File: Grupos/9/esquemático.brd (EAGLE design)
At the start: 70.1 x 59.1 mm, 28 parts, among them Q1 MMBT4403LT1SMD, Q3 MMBT4403LT1SMD, U3 AP2210N-4.0TRG1, X1 MKDSN1,5/2-5,08, X2 MKDSN1,5/2-5,08, X3 MKDSN1,5/2-5,08, X4 MKDSN1,5/2-5,08

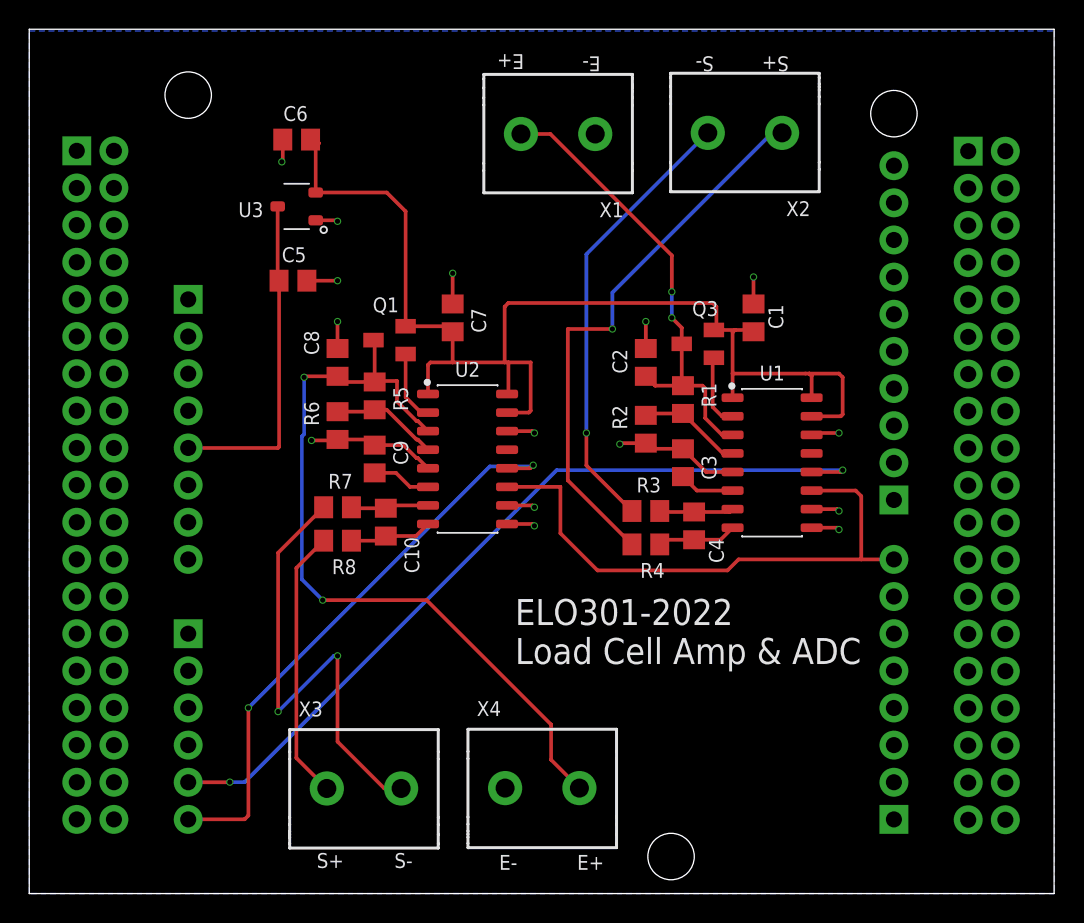
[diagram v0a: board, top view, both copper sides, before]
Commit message: Se cablean los ADC a SPI1 y SPI2
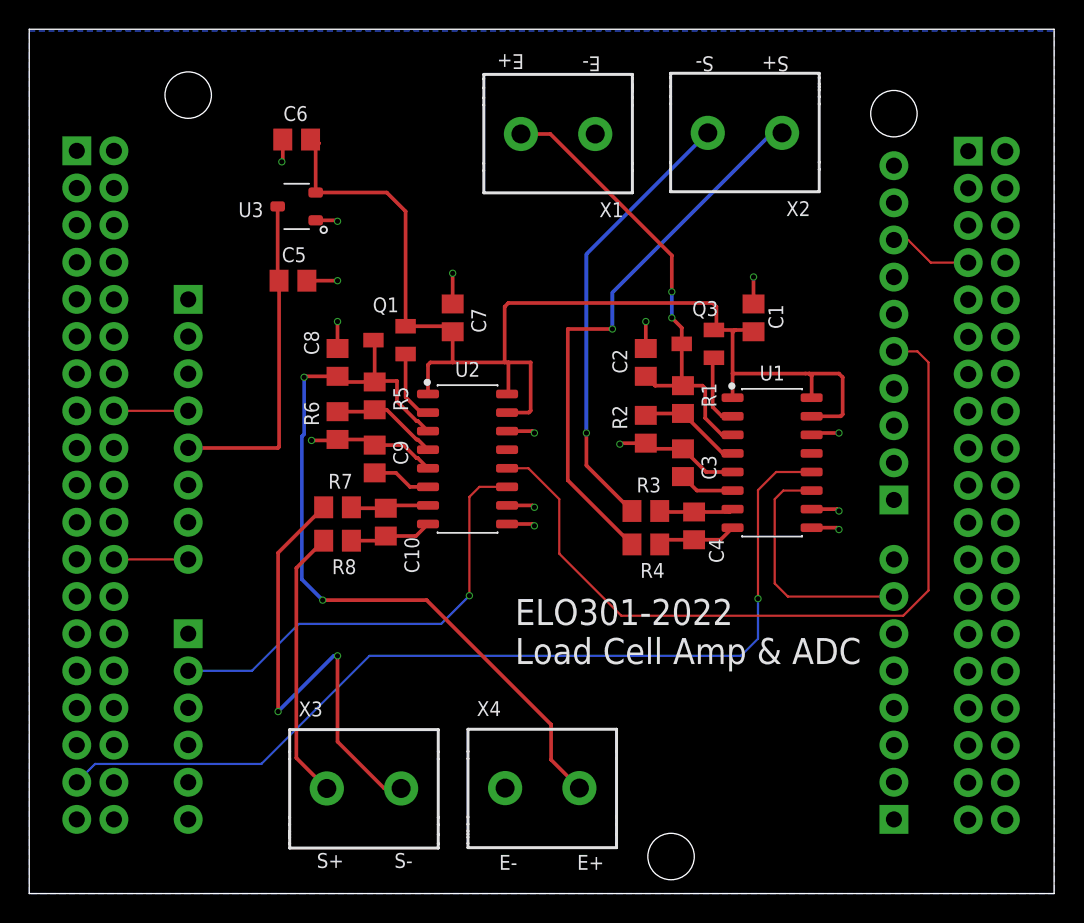
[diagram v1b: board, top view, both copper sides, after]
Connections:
- removed net N$20: M1.CN8-6, U2.12
- new net N$17: M1.CN5-5, U2.12
- new net N$21: M1.CN8-2, U2.11
- net N$19: now also M1.CN7-35; no longer M1.CN8-5
- net N$3: now also M1.CN9-7; no longer M1.CN9-8, U2.11
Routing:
- net N$17: track 0.00 -> 54.2 mm
- net N$20: track 40.0 -> 0.00 mm, vias 2 -> 0
- net N$21: track 0.00 -> 31.0 mm, vias 0 -> 1
- net N$3: track 38.9 -> 17.1 mm
- net N$19: track 55.8 -> 65.0 mm, vias 2 -> 1
- net AVDD: track 0.00 -> 5.72 mm
- net VIN: track 0.00 -> 5.08 mm
- net +3V3: track 0.00 -> 5.08 mm
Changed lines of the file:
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@@
 <contactref element="M1" pad="CN7-16"/>
 <contactref element="M1" pad="CN6-4"/>
-<wire x1="5.79" y1="33.012" x2="10.87" y2="33.012" width="0" layer="19" extent="1-1"/>
+<wire x1="5.79" y1="33.012" x2="10.87" y2="33.012" width="0.1524" layer="1"/>
 </signal>
 <signal name="+5V">
@@
 <contactref element="M1" pad="CN7-24"/>
 <contactref element="M1" pad="CN6-8"/>
-<wire x1="5.79" y1="22.852" x2="10.87" y2="22.852" width="0" layer="19" extent="1-1"/>
+<wire x1="5.79" y1="22.852" x2="10.87" y2="22.852" width="0.1524" layer="1"/>
 </signal>
 <signal name="VBAT">
@@
 <contactref element="M1" pad="CN5-8"/>
 <contactref element="M1" pad="CN10-7"/>
-<wire x1="59.13" y1="44.696" x2="64.21" y2="43.14700625" width="0" layer="19" extent="1-1"/>
+<wire x1="59.13" y1="44.696" x2="60.1044" y2="44.696" width="0.1524" layer="1"/>
+<wire x1="61.65339375" y1="43.14700625" x2="64.21" y2="43.14700625" width="0.1524" layer="1"/>
+<wire x1="60.1044" y1="44.696" x2="61.65339375" y2="43.14700625" width="0.1524" layer="1"/>
 </signal>
 <signal name="U5V">
@@
 <wire x1="25.738" y1="33.952" x2="25.738" y2="36.896" width="0.254" layer="1"/>
 <wire x1="26.67" y1="33.02" x2="25.738" y2="33.952" width="0.254" layer="1"/>
-</signal>
-<signal name="N$3">
-<contactref element="M1" pad="CN9-8"/>
-<contactref element="U1" pad="11"/>
-<contactref element="U2" pad="11"/>
-<wire x1="59.13" y1="22.852" x2="56.896" y2="22.852" width="0.254" layer="1"/>
-<wire x1="56.896" y1="22.852" x2="48.506" y2="22.852" width="0.254" layer="1"/>
-<wire x1="47.752" y1="22.098" x2="38.862" y2="22.098" width="0.254" layer="1"/>
-<wire x1="38.862" y1="22.098" x2="36.322" y2="24.638" width="0.254" layer="1"/>
-<wire x1="36.322" y1="24.638" x2="36.322" y2="27.813" width="0.254" layer="1"/>
-<wire x1="36.322" y1="27.813" x2="32.6753" y2="27.813" width="0.254" layer="1"/>
-<wire x1="48.506" y1="22.852" x2="47.752" y2="22.098" width="0.254" layer="1"/>
-<wire x1="53.5033" y1="27.559" x2="56.515" y2="27.559" width="0.254" layer="1"/>
-<wire x1="56.896" y1="27.178" x2="56.896" y2="22.852" width="0.254" layer="1"/>
-<wire x1="56.515" y1="27.559" x2="56.896" y2="27.178" width="0.254" layer="1"/>
-</signal>
-<signal name="N$19">
-<contactref element="U1" pad="12"/>
-<contactref element="M1" pad="CN8-5"/>
-<wire x1="10.87" y1="7.612" x2="13.708" y2="7.612" width="0.254" layer="1"/>
-<wire x1="13.708" y1="7.612" x2="13.716" y2="7.62" width="0.254" layer="1"/>
-<via x="13.716" y="7.62" extent="1-16" drill="0.35"/>
-<wire x1="13.716" y1="7.62" x2="14.732" y2="7.62" width="0.254" layer="16"/>
-<wire x1="36.068" y1="28.956" x2="14.732" y2="7.62" width="0.254" layer="16"/>
-<wire x1="36.068" y1="28.956" x2="55.626" y2="28.956" width="0.254" layer="16"/>
-<via x="55.626" y="28.956" extent="1-16" drill="0.35"/>
-<wire x1="55.626" y1="28.956" x2="55.499" y2="28.829" width="0.254" layer="1"/>
-<wire x1="55.499" y1="28.829" x2="53.5033" y2="28.829" width="0.254" layer="1"/>
-</signal>
-<signal name="N$20">
-<contactref element="M1" pad="CN8-6"/>
-<contactref element="U2" pad="12"/>
-<wire x1="10.87" y1="5.072" x2="10.878" y2="5.08" width="0.254" layer="1"/>
-<wire x1="10.878" y1="5.08" x2="14.732" y2="5.08" width="0.254" layer="1"/>
-<wire x1="14.732" y1="5.08" x2="14.986" y2="5.334" width="0.254" layer="1"/>
-<wire x1="14.986" y1="5.334" x2="14.986" y2="12.7" width="0.254" layer="1"/>
-<via x="14.986" y="12.7" extent="1-16" drill="0.35"/>
-<wire x1="31.496" y1="29.21" x2="32.512" y2="29.21" width="0.254" layer="16"/>
-<wire x1="14.986" y1="12.7" x2="31.496" y2="29.21" width="0.254" layer="16"/>
-<wire x1="32.512" y1="29.21" x2="34.544" y2="29.21" width="0.254" layer="16"/>
-<wire x1="34.544" y1="29.21" x2="34.46000625" y2="29.29399375" width="0.254" layer="16"/>
-<via x="34.46000625" y="29.29399375" extent="1-16" drill="0.35"/>
-<wire x1="34.46000625" y1="29.29399375" x2="34.2490125" y2="29.083" width="0.254" layer="1"/>
-<wire x1="34.2490125" y1="29.083" x2="32.6753" y2="29.083" width="0.254" layer="1"/>
 </signal>
 <signal name="N$22">
@@
 <wire x1="55.372" y1="35.56" x2="53.34" y2="35.56" width="0.254" layer="1"/>
 </signal>
+<signal name="N$17">
+<contactref element="U2" pad="12"/>
+<contactref element="M1" pad="CN5-5"/>
+<wire x1="59.13" y1="37.076" x2="60.7394" y2="37.076" width="0.1524" layer="1"/>
+<wire x1="60.7394" y1="37.076" x2="61.4934" y2="36.322" width="0.1524" layer="1"/>
+<wire x1="61.4934" y1="36.322" x2="61.4934" y2="20.7264" width="0.1524" layer="1"/>
+<wire x1="61.4934" y1="20.7264" x2="59.7662" y2="18.9992" width="0.1524" layer="1"/>
+<wire x1="34.1376" y1="29.083" x2="32.6753" y2="29.083" width="0.1524" layer="1"/>
+<wire x1="59.7662" y1="18.9992" x2="40.4876" y2="18.9992" width="0.1524" layer="1"/>
+<wire x1="40.4876" y1="18.9992" x2="36.2458" y2="23.241" width="0.1524" layer="1"/>
+<wire x1="36.2458" y1="23.241" x2="36.2458" y2="26.9748" width="0.1524" layer="1"/>
+<wire x1="36.2458" y1="26.9748" x2="34.1376" y2="29.083" width="0.1524" layer="1"/>
+</signal>
+<signal name="N$21">
+<contactref element="U2" pad="11"/>
+<contactref element="M1" pad="CN8-2"/>
+<wire x1="10.87" y1="15.232" x2="15.232" y2="15.232" width="0.1524" layer="16"/>
+<wire x1="28.1686" y1="18.4404" x2="30.099" y2="20.3708" width="0.1524" layer="16"/>
+<via x="30.099" y="20.3708" extent="1-16" drill="0.35"/>
+<wire x1="30.099" y1="20.3708" x2="30.099" y2="27.1272" width="0.1524" layer="1"/>
+<wire x1="30.7848" y1="27.813" x2="32.6753" y2="27.813" width="0.1524" layer="1"/>
+<wire x1="15.232" y1="15.232" x2="18.4404" y2="18.4404" width="0.1524" layer="16"/>
+<wire x1="18.4404" y1="18.4404" x2="28.1686" y2="18.4404" width="0.1524" layer="16"/>
+<wire x1="30.099" y1="27.1272" x2="30.7848" y2="27.813" width="0.1524" layer="1"/>
+</signal>
+<signal name="N$3">
+<contactref element="U1" pad="11"/>
+<contactref element="M1" pad="CN9-7"/>
+<wire x1="59.13" y1="20.312" x2="51.8748" y2="20.312" width="0.1524" layer="1"/>
+<wire x1="51.8748" y1="20.312" x2="50.9778" y2="21.209" width="0.1524" layer="1"/>
+<wire x1="50.9778" y1="21.209" x2="50.9778" y2="26.9748" width="0.1524" layer="1"/>
+<wire x1="51.562" y1="27.559" x2="53.5033" y2="27.559" width="0.1524" layer="1"/>
+<wire x1="50.9778" y1="26.9748" x2="51.562" y2="27.559" width="0.1524" layer="1"/>
+</signal>
+<signal name="N$19">
+<contactref element="M1" pad="CN7-35"/>
+<contactref element="U1" pad="12"/>
+<wire x1="3.25" y1="7.612" x2="4.5026" y2="8.8646" width="0.1524" layer="16"/>
+<wire x1="23.2664" y1="16.256" x2="48.6664" y2="16.256" width="0.1524" layer="16"/>
+<wire x1="48.6664" y1="16.256" x2="49.8348" y2="17.4244" width="0.1524" layer="16"/>
+<wire x1="49.8348" y1="17.4244" x2="49.8348" y2="20.1676" width="0.1524" layer="16"/>
+<via x="49.8348" y="20.1676" extent="1-16" drill="0.35"/>
+<wire x1="49.8348" y1="20.1676" x2="49.8348" y2="27.5844" width="0.1524" layer="1"/>
+<wire x1="51.0794" y1="28.829" x2="53.5033" y2="28.829" width="0.1524" layer="1"/>
+<wire x1="4.5026" y1="8.8646" x2="15.875" y2="8.8646" width="0.1524" layer="16"/>
+<wire x1="15.875" y1="8.8646" x2="23.2664" y2="16.256" width="0.1524" layer="16"/>
+<wire x1="49.8348" y1="27.5844" x2="51.0794" y2="28.829" width="0.1524" layer="1"/>
+</signal>
 </signals>
